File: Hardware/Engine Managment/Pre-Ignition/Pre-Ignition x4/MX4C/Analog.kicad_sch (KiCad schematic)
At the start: 57 parts, among them J4 Map/Baro Sensor Socket, J6 VR_Header, Q10 AO3400A, Q11 AO3400A, Q9 AO3400A, U1 SRV05-4-P-T7, U4 SRV05-4-P-T7, U5 SRV05-4-P-T7

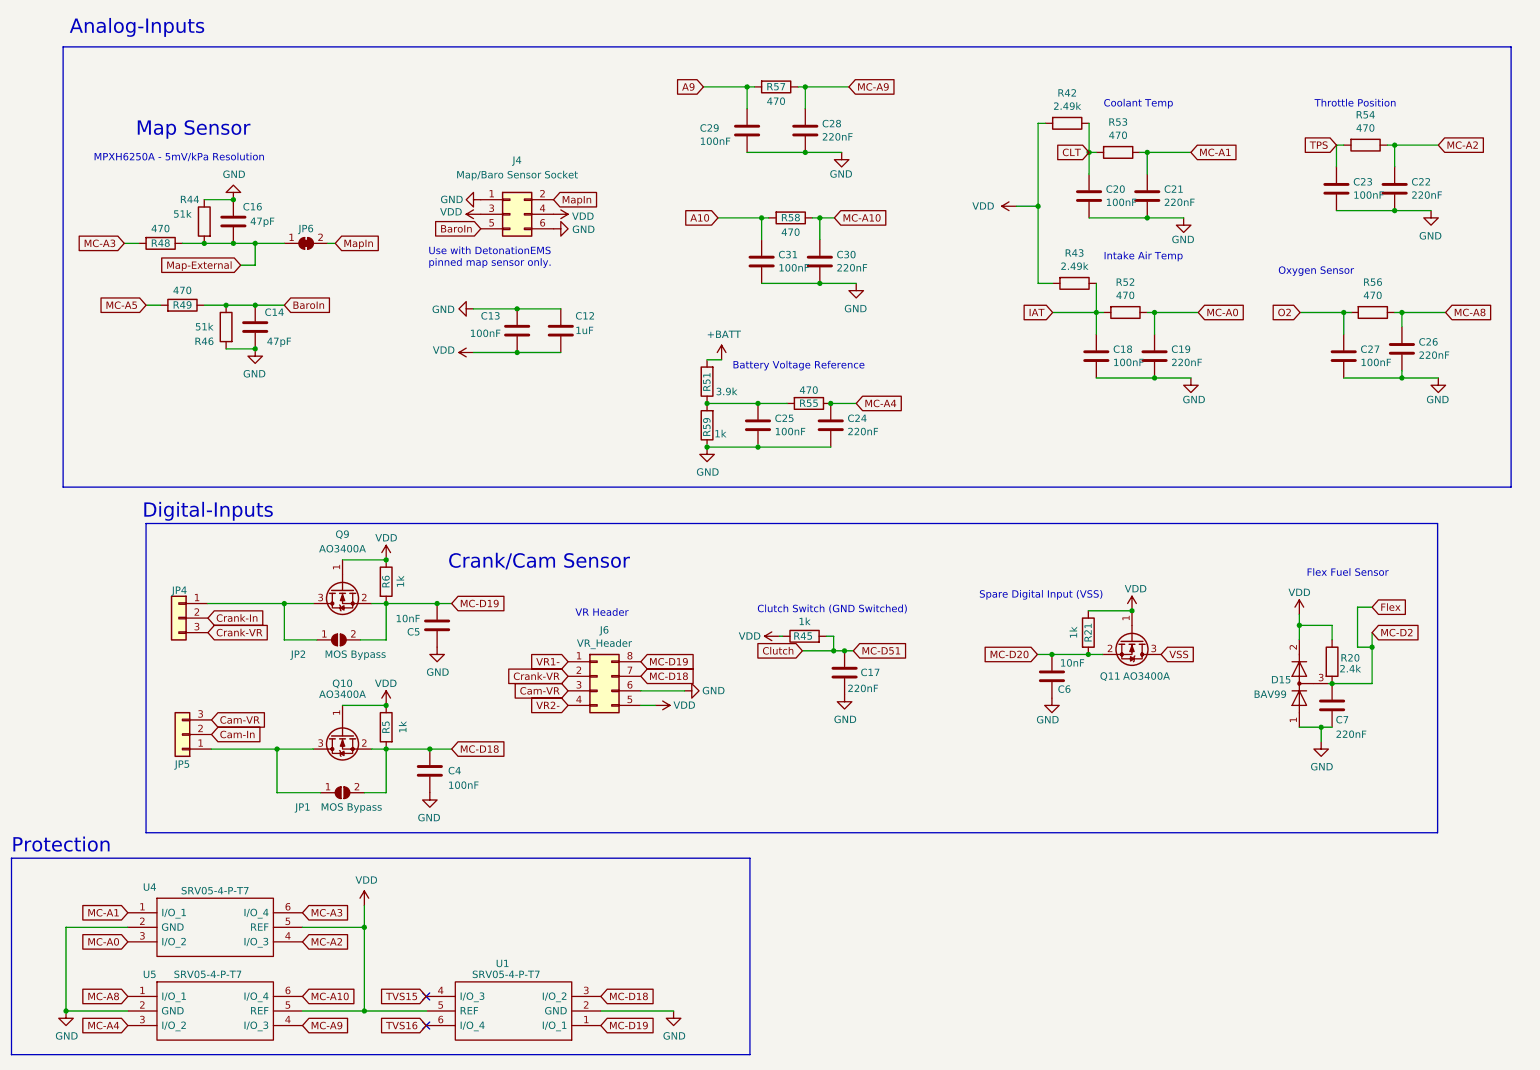
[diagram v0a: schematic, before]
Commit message: Upload correct initial upload files
Initial upload files were accidently taken from an alpha folder. 5v pins on main connector had no voltage. To fix the issue on any manufactured boards remove C8 and C9. Then short the pins of the removed capacitors.
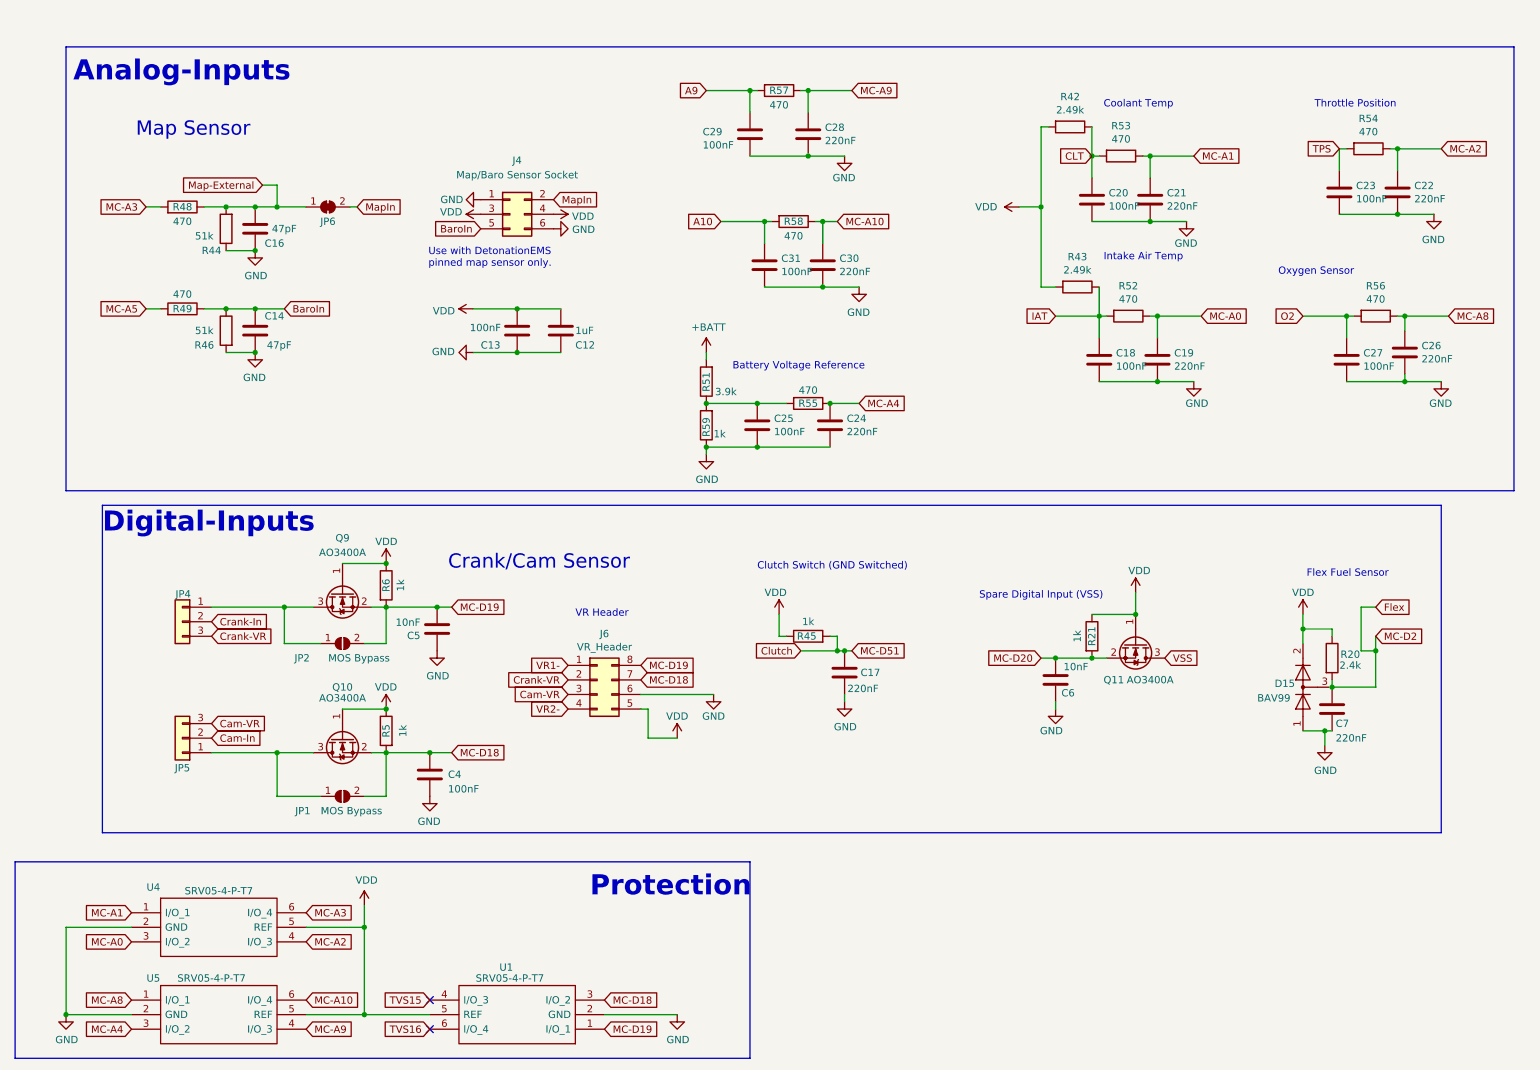
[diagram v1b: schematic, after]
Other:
- note removed: "MPXH6250A - 5mV/kPa Resolution"
- moved on the sheet: C14, C16, C18, C19, C20, C21, C22, C23, C26, C27, C28, C29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

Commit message: Structure Update
MX2 - RevB Upload
MX4B-2 - KiCad Version update (no changes)
MX4C - Organized Schematic, Minor layout change
Engine Simulator 8 Channel - Organized Schematic (no changes)
PMAP-M - Map Sensor Breakout for MX4C
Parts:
- renumbered C12 to C11, C13 to C12, C14 to C13, C16 to C14, C17 to C15, C18 to C16, C19 to C17, C20 to C18, C21 to C19, C22 to C20, C23 to C21, C24 to C22, C25 to C23, C26 to C24, C27 to C25, C28 to C26, C29 to C27, C30 to C28, C31 to C29, C4 to C5, C5 to C6, C6 to C7, C7 to C8, D15 to D16, J6 to J5, J4 to J7, JP2 to JP1, JP1 to JP2, JP6 to JP3, JP5 to JP4, JP4 to JP5, Q9 to Q10, Q10 to Q9, R5 to R1, R6 to R2, R51 to R52, R52 to R53, R53 to R54, R54 to R55, R55 to R56, R56 to R57, R57 to R58, R58 to R59, R59 to R60
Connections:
- net VDD renamed +5V
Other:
- note added: "5v Protection"
- note added: "Aux Analog"
- note added: "Crank/Cam Inputs"
- note added: "Primary Analog"
- note added: "VR Header (Speeduino Compatible)"
- note removed: "Crank/Cam Sensor"
- note removed: "Protection"
- note removed: "VR Header"
- moved on the sheet: C11, C12, C13, C14, C15, C16, C17, C18, C19, C20, C21, C22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

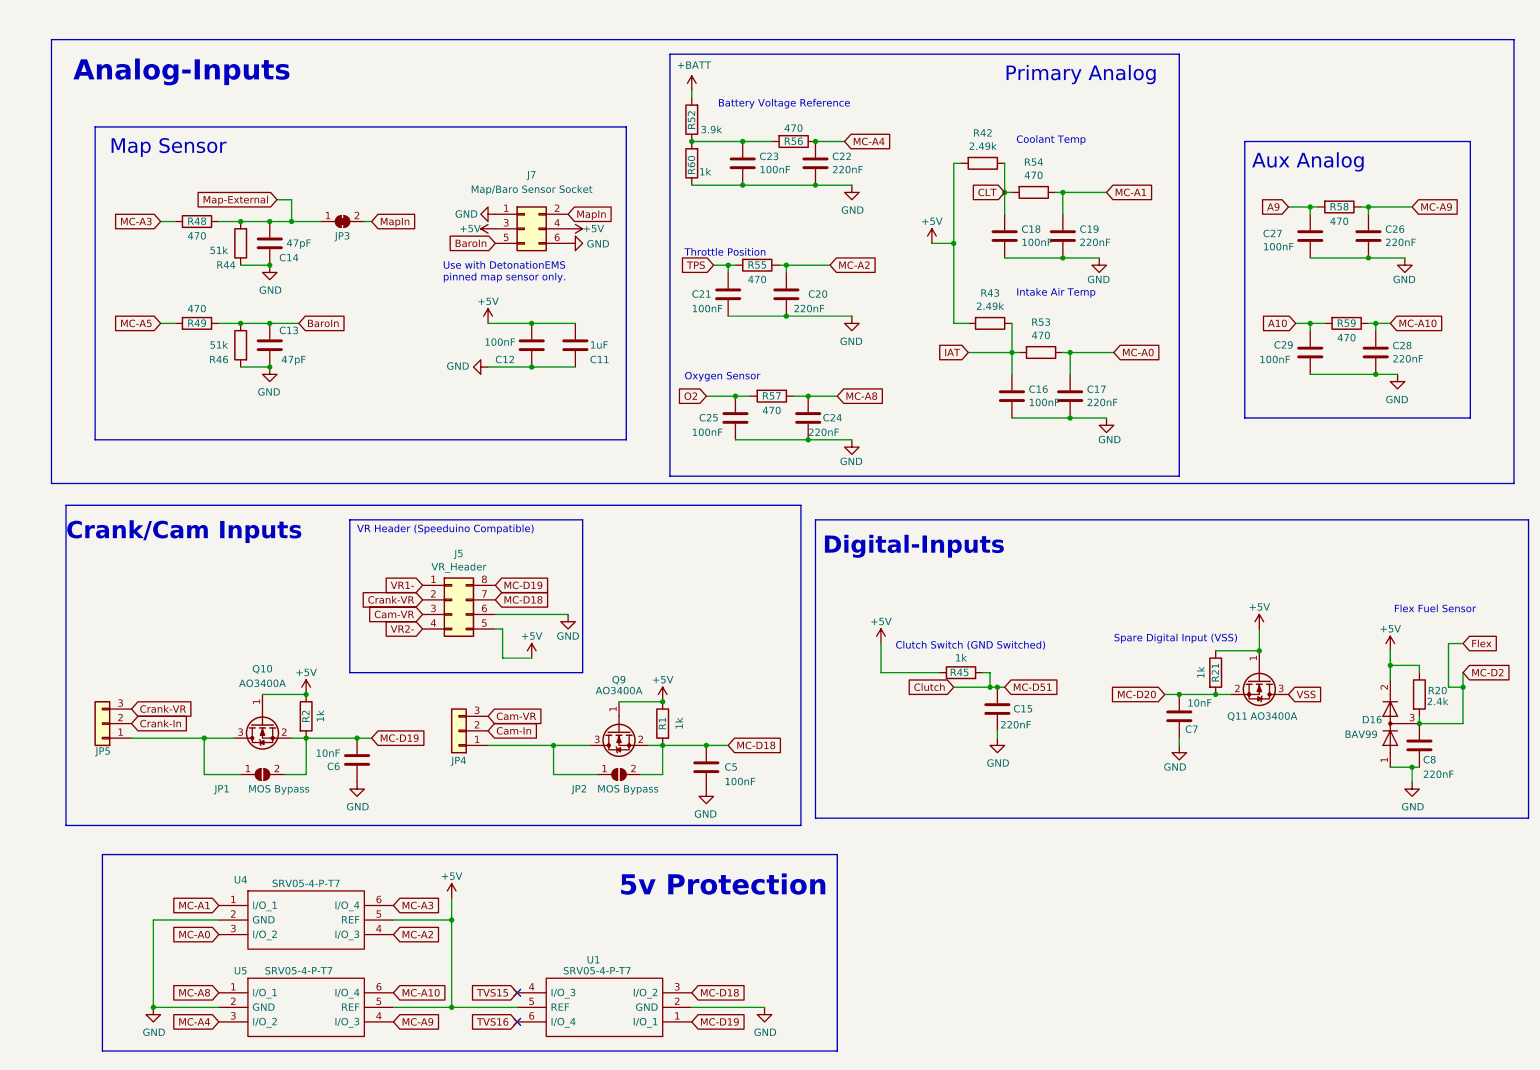
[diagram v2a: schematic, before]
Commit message: minor update
Copper Pour and clearances updated.
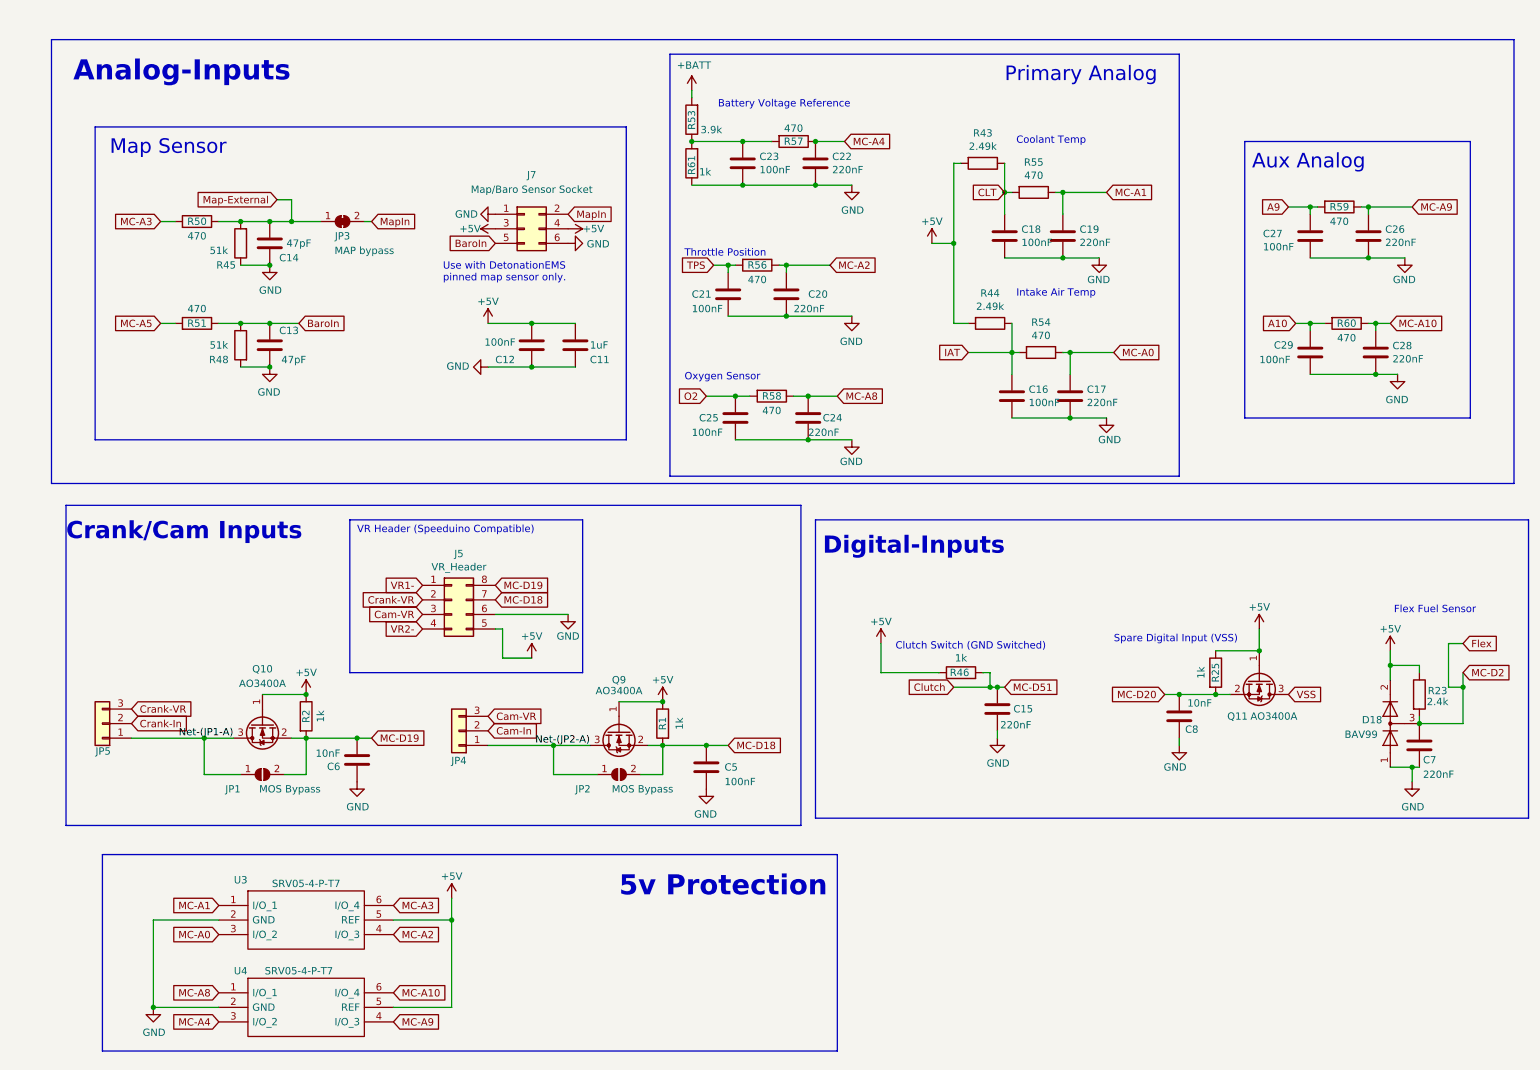
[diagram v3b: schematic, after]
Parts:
- removed U1: SRV05-4-P-T7, Package_TO_SOT_SMD:SOT-23-6, symbol Pre_Ignition-rescue:SRV05-4-P-T7-SRV05-4-P-T7-Pre_Ignition-rescue-Pre_Ignition-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
- J5: footprint Detonation:Socket_VRConditioner -> Detonation:Socket_VRConditioner_Corrected
- JP3: value SolderJumper_2_Bridged -> MAP bypass
- JP4, JP5: footprint Detonation:1x03_Horizontal_2.54mm -> Detonation:1x03-Proto
- renumbered C8 to C7, C7 to C8, D16 to D18, R20 to R23, R21 to R25, R42 to R43, R43 to R44, R44 to R45, R45 to R46, R46 to R48, R48 to R50, R49 to R51, R52 to R53, R53 to R54, R54 to R55, R55 to R56, R56 to R57, R57 to R58, R58 to R59, R59 to R60, R60 to R61, U4 to U3, U5 to U4
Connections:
- net Net-(JP1-A): now reaches JP1.1 (A), JP5.1 (Pin_1), Q10.3 (D)
- net Net-(JP2-A): now reaches JP2.1 (A), JP4.1 (Pin_1), Q9.3 (D)
- no-connect marks 2 -> 0
